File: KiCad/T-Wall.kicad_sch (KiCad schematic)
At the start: 52 parts, among them J1 IDC, J2 IDC, J3 IDC, J4 IDC, J5 IDC, J6 IDC, J7 IDC, J8 IDC, J9 2086-1107/300-000/997-607, U1 TCA9555PWR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

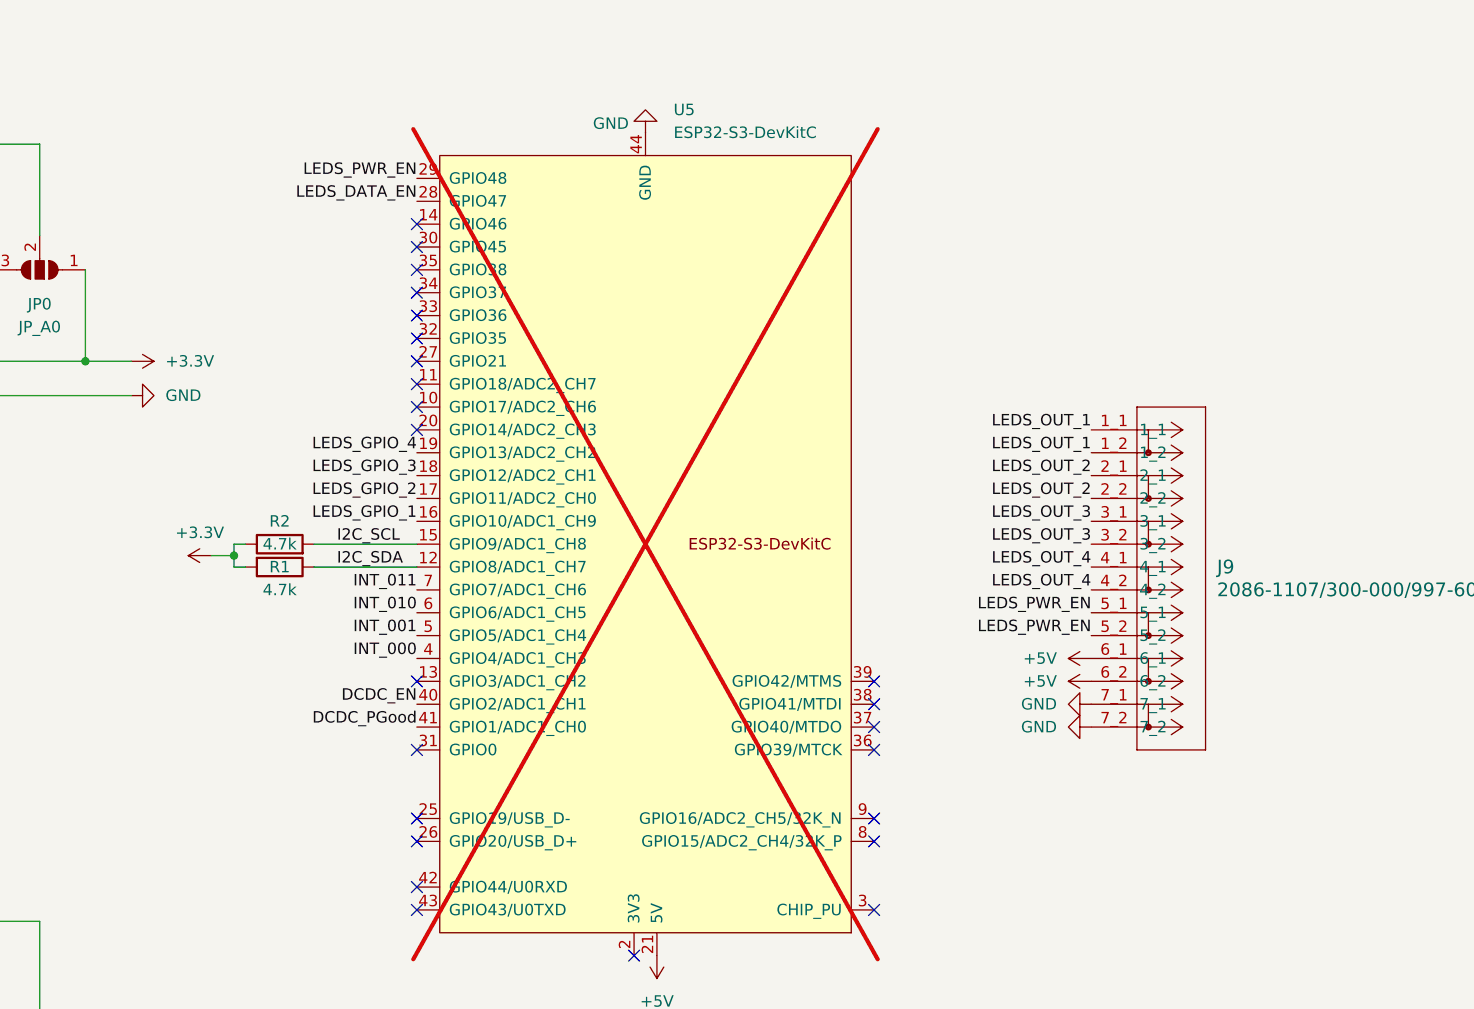
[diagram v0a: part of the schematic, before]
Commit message: PCB: routed unused GPIOs to Pins
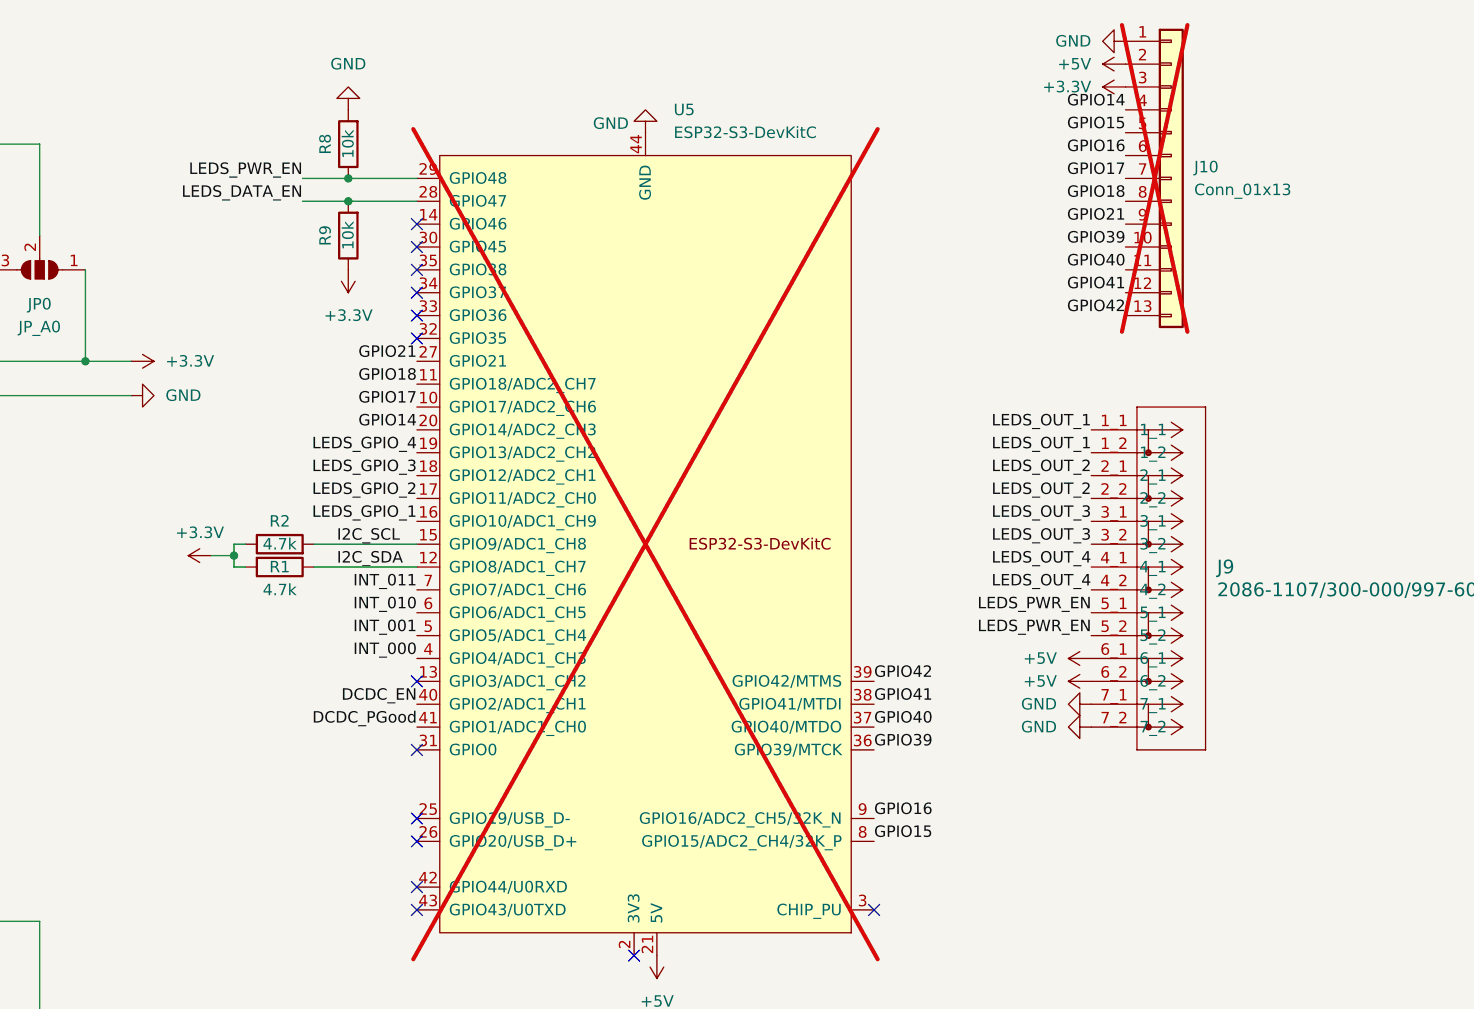
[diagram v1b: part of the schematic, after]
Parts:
- added J10: Conn_01x13, Connector_PinHeader_2.54mm:PinHeader_1x13_P2.54mm_Vertical, symbol Connector_Generic:Conn_01x13
- added R8, R9: 10k, Resistor_SMD:R_0603_1608Metric_Pad0.98x0.95mm_HandSolder, symbol Device:R
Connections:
- net +3.3V: now also J10.3 (Pin_3), R9.1
- net +5V: now also J10.2 (Pin_2)
- net GND: now also J10.1 (Pin_1), R8.2
- net LEDS_DATA_EN: now also R9.2
- net LEDS_PWR_EN: now also R8.1
- net GPIO17: now reaches U5.10 (GPIO17/ADC2_CH6)
- net GPIO17: now also J10.7 (Pin_7)
- net GPIO18: now reaches U5.11 (GPIO18/ADC2_CH7)
- net GPIO18: now also J10.8 (Pin_8)
- net GPIO14: now reaches U5.20 (GPIO14/ADC2_CH3)
- net GPIO14: now also J10.4 (Pin_4)
- net GPIO21: now reaches U5.27 (GPIO21)
- net GPIO21: now also J10.9 (Pin_9)
- net GPIO39: now reaches U5.36 (GPIO39/MTCK)
- net GPIO39: now also J10.10 (Pin_10)
- net GPIO40: now reaches U5.37 (GPIO40/MTDO)
- net GPIO40: now also J10.11 (Pin_11)
- net GPIO41: now reaches U5.38 (GPIO41/MTDI)
- net GPIO41: now also J10.12 (Pin_12)
- net GPIO42: now reaches U5.39 (GPIO42/MTMS)
- net GPIO42: now also J10.13 (Pin_13)
- net GPIO15: now reaches U5.8 (GPIO15/ADC2_CH4/32K_P)
- net GPIO15: now also J10.5 (Pin_5)
- net GPIO16: now reaches U5.9 (GPIO16/ADC2_CH5/32K_N)
- net GPIO16: now also J10.6 (Pin_6)
- no-connect marks 24 -> 14

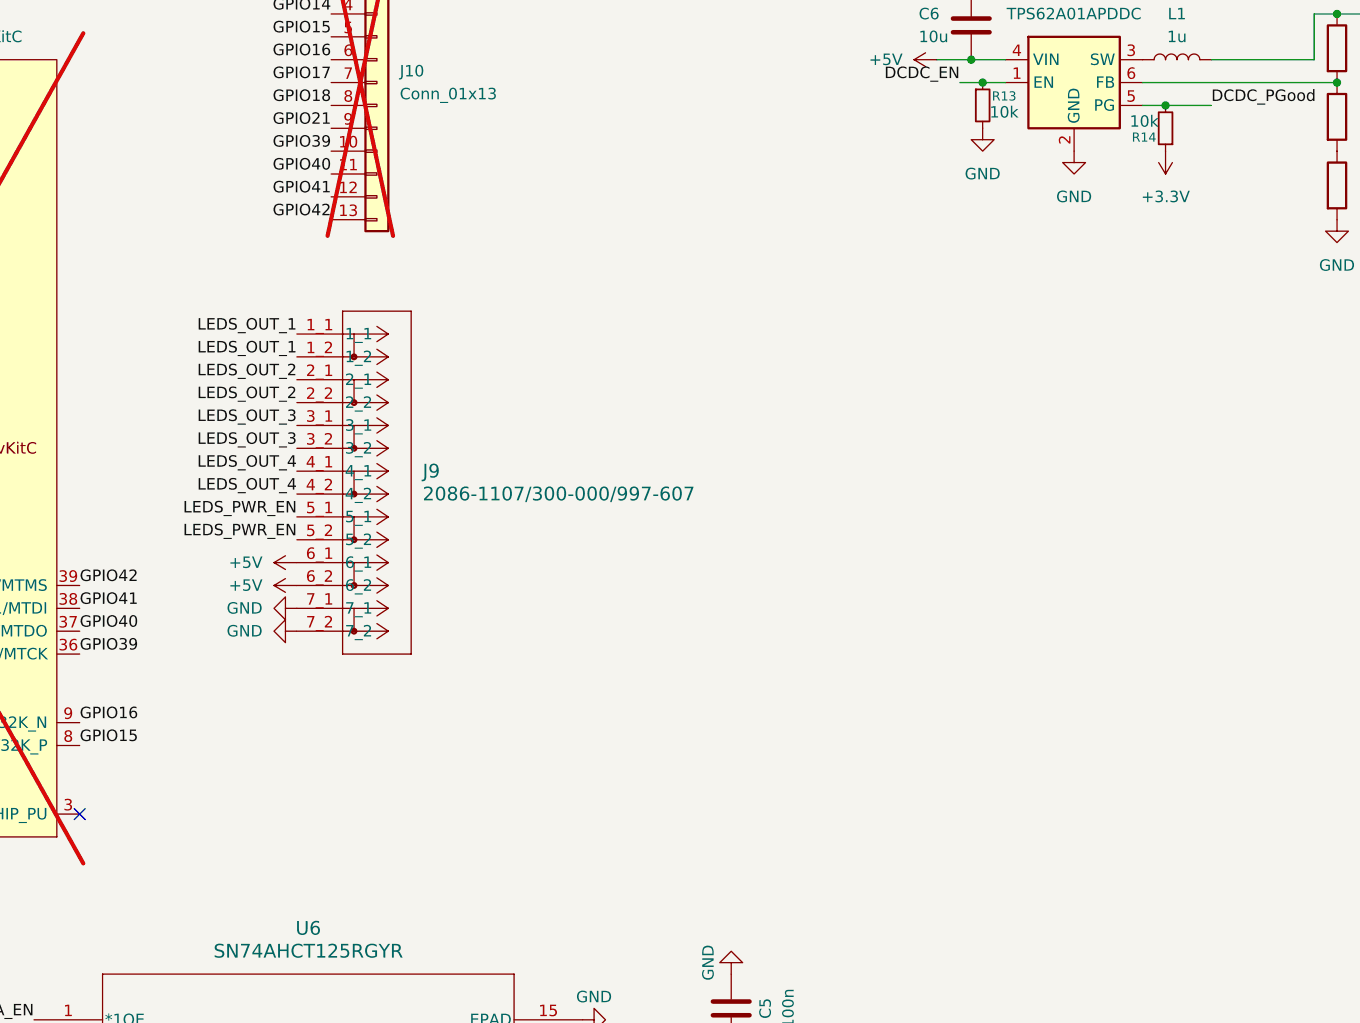
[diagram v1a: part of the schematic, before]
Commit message: PCB: added fuse and reverse-polarity-protection
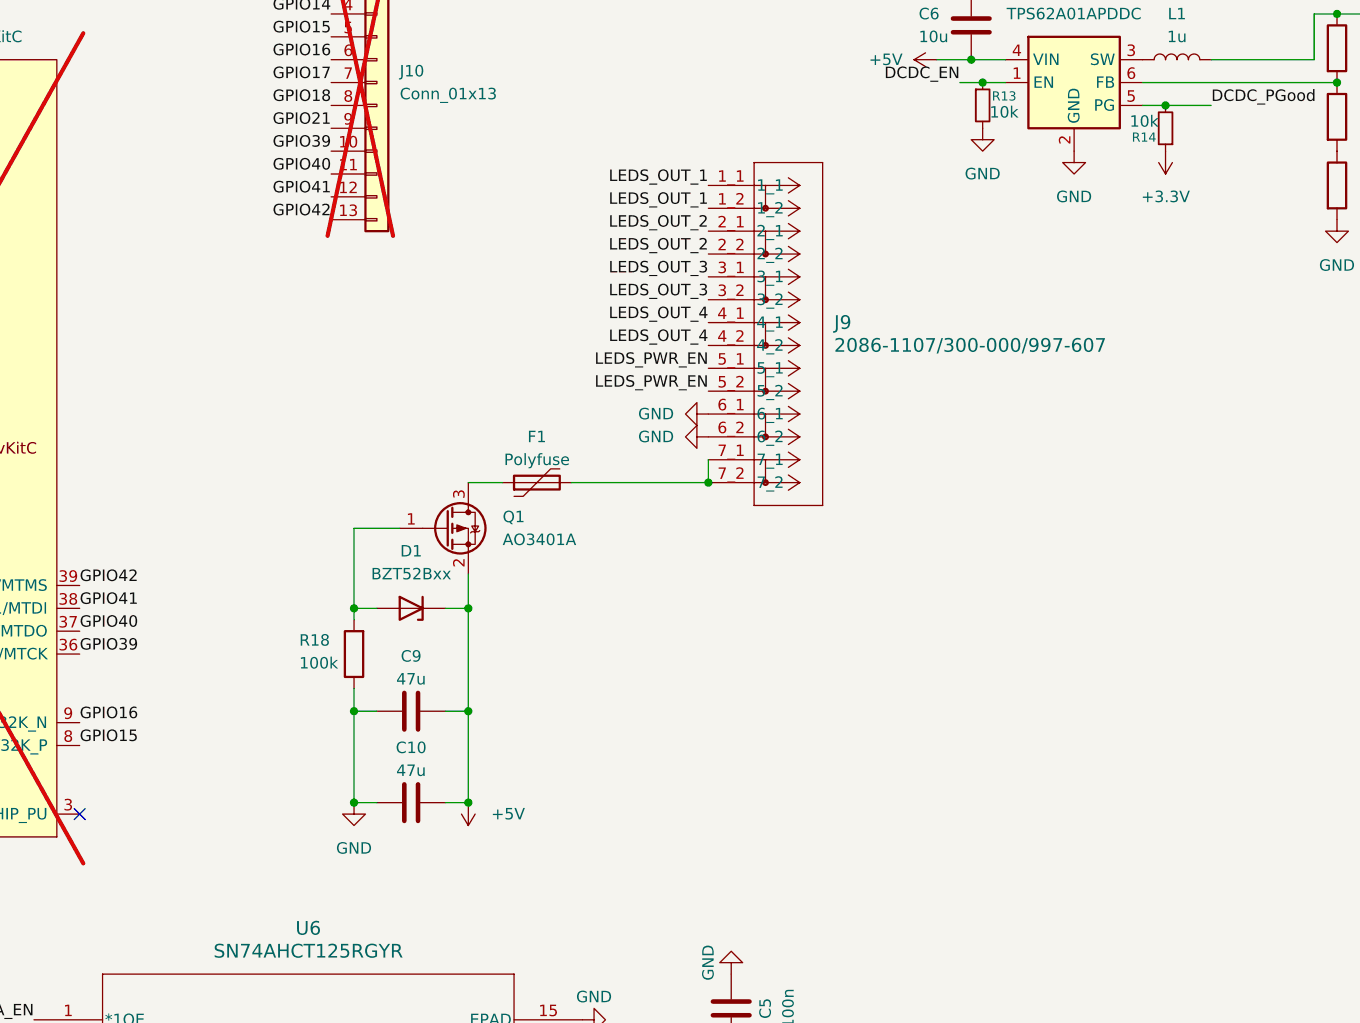
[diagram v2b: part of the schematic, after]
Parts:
- added C10, C9: 47u, Capacitor_SMD:C_1206_3216Metric_Pad1.33x1.80mm_HandSolder, symbol Device:C
- added D1: BZT52Bxx, Diode_SMD:D_SOD-123F, symbol Diode:BZT52Bxx
- added F1: Polyfuse, Fuse:Fuse_1206_3216Metric_Pad1.42x1.75mm_HandSolder, symbol Device:Polyfuse
- added Q1: AO3401A, Package_TO_SOT_SMD:SOT-23, symbol Transistor_FET:AO3401A
- added R18: 100k, Resistor_SMD:R_0603_1608Metric_Pad0.98x0.95mm_HandSolder, symbol Device:R
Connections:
- net +5V: now also C10.2, C9.2, D1.1 (K), Q1.2 (S); no longer J9.6_1, J9.6_2
- net GND: now also J9.6_1, J9.6_2, C10.1, C9.1, R18.1; no longer J9.7_1, J9.7_2
- new net: D1.2 (A), Q1.1 (G), R18.2
- new net: F1.2, J9.7_1, J9.7_2
- new net: F1.1, Q1.3 (D)
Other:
- moved on the sheet: J9

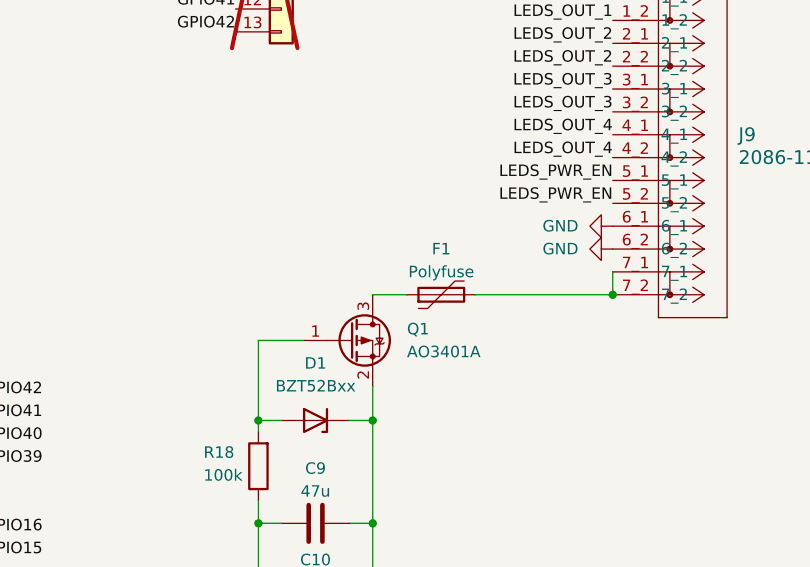
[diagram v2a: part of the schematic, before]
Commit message: PCB: overvoltage-protection and optimized routing
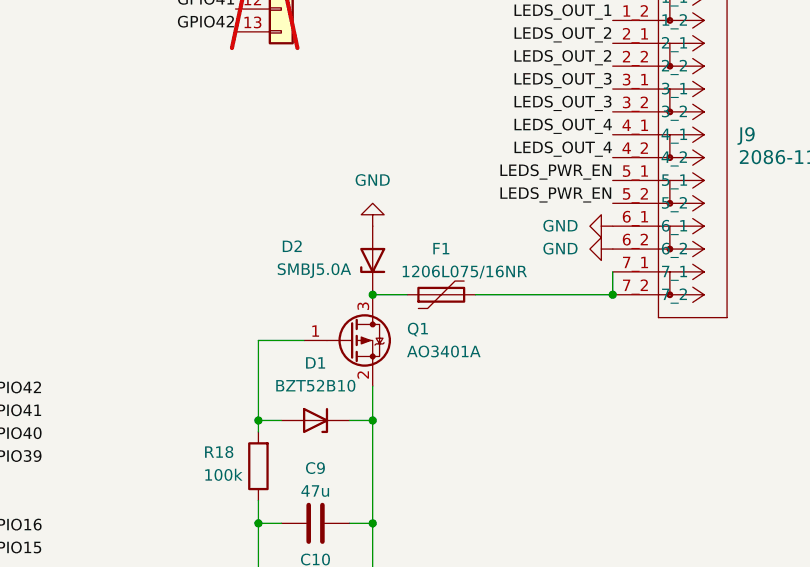
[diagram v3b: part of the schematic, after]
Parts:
- added D2: SMBJ5.0A, Diode_SMD:D_SMB_Handsoldering, symbol Device:D_Zener
- D1: value BZT52Bxx -> BZT52B10
- F1: value Polyfuse -> 1206L075/16NR
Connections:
- net GND: now also D2.2 (A)
- net at F1.1, Q1.3 (D): now also D2.1 (K)
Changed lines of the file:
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@@
 	)
 	(junction
+		(at 290.83 85.09)
+		(diameter 0)
+		(color 0 0 0 0)
+	)
+	(junction
 		(at 189.23 43.18)
 		(diameter 0)
@@
 	)
 	(symbol
+		(lib_id "Device:D_Zener")
+		(at 290.83 81.28 90)
+		(unit 1)
+		(exclude_from_sim no)
+		(in_bom yes)
+		(on_board yes)
+		(dnp no)
+		(property "Reference" "D2"
+			(at 280.67 79.756 90)
+			(effects
+				(font
+					(size 1.27 1.27)
+				)
+				(justify right)
+			)
+		)
+		(property "Value" "SMBJ5.0A"
+			(at 280.162 82.296 90)
+			(effects
+				(font
+					(size 1.27 1.27)
+				)
+				(justify right)
+			)
+		)
+		(property "Footprint" "Diode_SMD:D_SMB_Handsoldering"
+			(at 290.83 81.28 0)
+			(effects
+				(font
+					(size 1.27 1.27)
+				)
+				(hide yes)
+			)
+		)
+		(property "Datasheet" "~"
+			(at 290.83 81.28 0)
+			(effects
+				(font
+					(size 1.27 1.27)
+				)
+				(hide yes)
+			)
+		)
+		(property "Description" "Zener diode"
+			(at 290.83 81.28 0)
+			(effects
+				(font
+					(size 1.27 1.27)
+				)
+				(hide yes)
+			)
+		)
+		(property "LCSC" "C19077558"
+			(at 290.83 81.28 90)
+			(effects
+				(font
+					(size 1.27 1.27)
+				)
+				(hide yes)
+			)
+		)
+		(pin "2"
+		)
+		(pin "1"
+		)
+		(instances
+			(project ""
+				(path "/7dc9e5b9-dd7a-4571-90c7-051ff63df3d4"
+					(reference "D2")
+					(unit 1)
+				)
+			)
+		)
+	)
+	(symbol
 		(lib_id "Device:R")
 		(at 224.79 157.48 270)
@@
 	)
 	(symbol
+		(lib_id "power:GND")
+		(at 290.83 77.47 180)
+		(unit 1)
+		(exclude_from_sim no)
+		(in_bom yes)
+		(on_board yes)
+		(dnp no)
+		(fields_autoplaced yes)
+		(property "Reference" "#PWR066"
+			(at 290.83 71.12 0)
+			(effects
+				(font
+					(size 1.27 1.27)
+				)
+				(hide yes)
+			)
+		)
+		(property "Value" "GND"
+			(at 290.83 72.39 0)
+			(effects
+				(font
+					(size 1.27 1.27)
+				)
+			)
+		)
+		(property "Footprint" ""
+			(at 290.83 77.47 0)
+			(effects
+				(font
+					(size 1.27 1.27)
+				)
+				(hide yes)
+			)
+		)
+		(property "Datasheet" ""
+			(at 290.83 77.47 0)
+			(effects
+				(font
+					(size 1.27 1.27)
+				)
+				(hide yes)
+			)
+		)
+		(property "Description" "Power symbol creates a global label with name \"GND\" , ground"
+			(at 290.83 77.47 0)
+			(effects
+				(font
+					(size 1.27 1.27)
+				)
+				(hide yes)
+			)
+		)
+		(pin "1"
+		)
+		(instances
+			(project "T-Wall"
+				(path "/7dc9e5b9-dd7a-4571-90c7-051ff63df3d4"
+					(reference "#PWR066")
+					(unit 1)
+				)
+			)
+		)
+	)
+	(symbol
 		(lib_id "Device:C")
 		(at 284.48 110.49 90)
@@
 			)
 		)
-		(property "Value" "Polyfuse"
-			(at 298.45 82.55 90)
+		(property "Value" "1206L075/16NR"
+			(at 300.99 82.55 90)
 			(effects
 				(font
@@
 			)
 		)
-		(property "Value" "BZT52Bxx"
+		(property "Value" "BZT52B10"
 			(at 284.48 95.25 0)
 			(effects
